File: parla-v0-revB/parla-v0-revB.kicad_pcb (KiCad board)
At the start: 2 copper layers, 70 x 70 mm, 0 parts

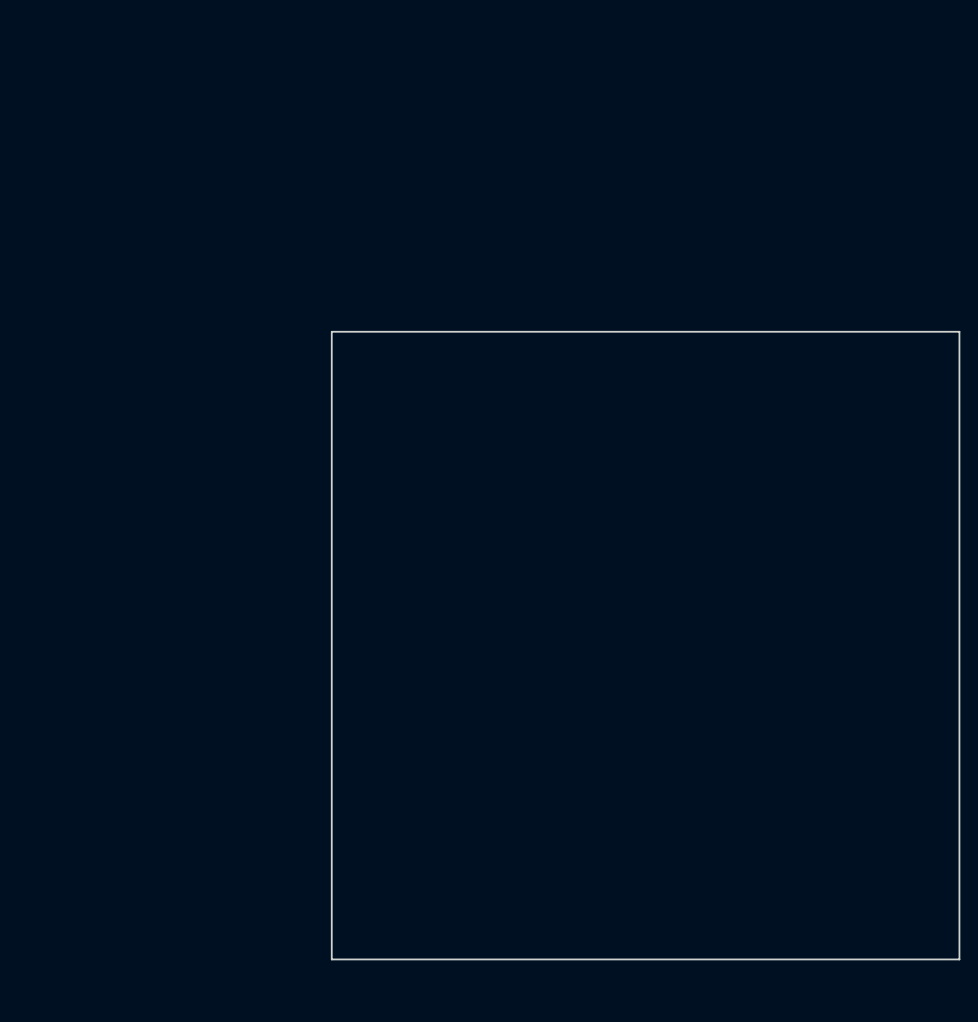
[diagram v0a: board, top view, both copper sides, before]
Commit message: agregar vias
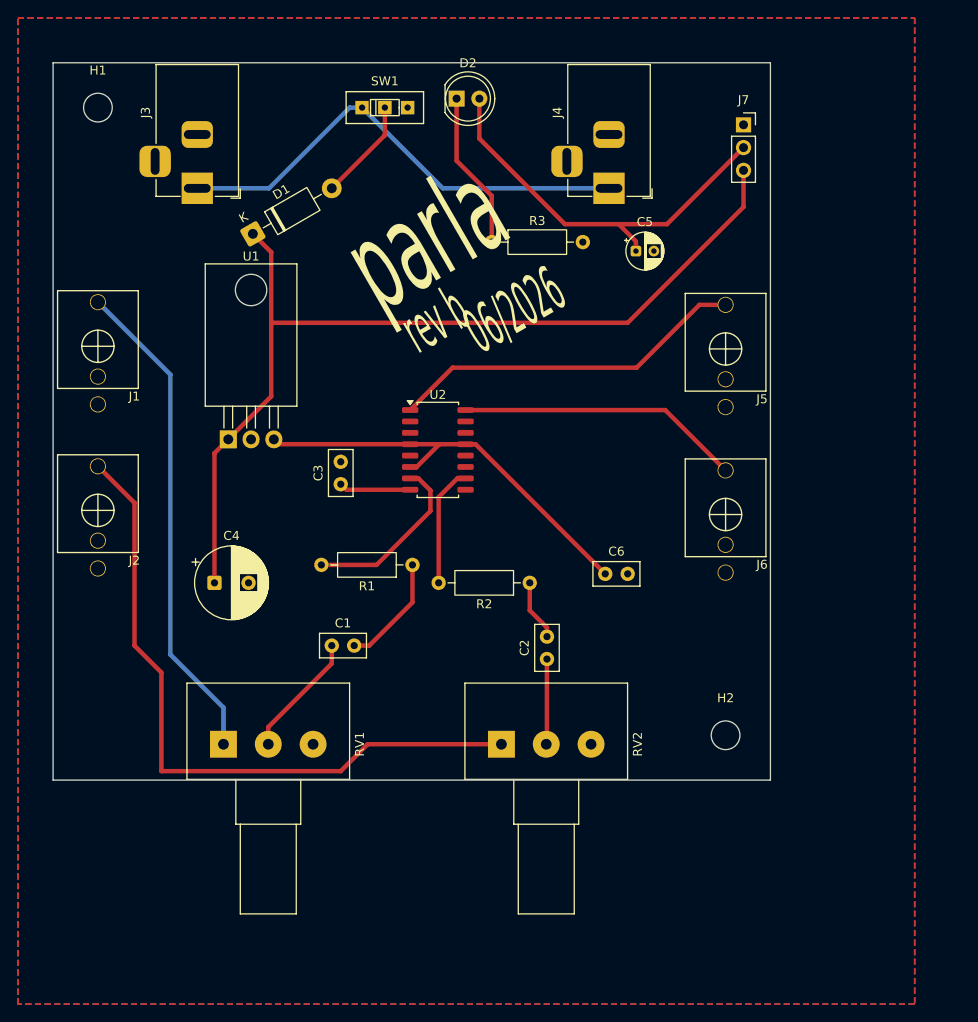
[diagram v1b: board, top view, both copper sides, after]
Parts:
- added C1: 470n, Capacitor_THT:C_Disc_D5.0mm_W2.5mm_P2.50mm, F.Cu at (50.0, 85.0)
- added C2: 470n, Capacitor_THT:C_Disc_D5.0mm_W2.5mm_P2.50mm, F.Cu at (74.0, 86.5)
- added C3: 100n, Capacitor_THT:C_Disc_D5.0mm_W2.5mm_P2.50mm, F.Cu at (51.0, 67.0)
- added C4: 100u, Capacitor_THT:CP_Radial_D8.0mm_P3.80mm, F.Cu at (36.9, 78.0)
- added C5: 10u, Capacitor_THT:CP_Radial_D4.0mm_P2.00mm, F.Cu at (83.9, 41.0)
- added C6: 100n, Capacitor_THT:C_Disc_D5.0mm_W2.5mm_P2.50mm, F.Cu at (80.5, 77.0)
- added D1: 1N4007, Diode_THT:D_DO-41_SOD81_P10.16mm_Horizontal, F.Cu at (41.2, 39.1)
- added D2: LED, LED_THT:LED_D5.0mm, F.Cu at (63.9, 24.0)
- added H1: M3, MountingHole:MountingHole_3.2mm_M3, F.Cu at (23.9, 25.0)
- added H2: M3, MountingHole:MountingHole_3.2mm_M3, F.Cu at (93.9, 95.0)
- added J1: AudioJack2_SwitchT, parla:PJ301M-12, F.Cu at (23.9, 51.6)
- added J2: AudioJack2_SwitchT, parla:PJ301M-12, F.Cu at (23.9, 69.9)
- added J3: Barrel_Jack_Switch, Connector_BarrelJack:BarrelJack_Horizontal, F.Cu at (35.0, 34.0)
- added J4: Barrel_Jack_Switch, Connector_BarrelJack:BarrelJack_Horizontal, F.Cu at (80.9, 34.0)
- added J5: AudioJack2_SwitchT, parla:PJ301M-12, F.Cu at (93.9, 51.9)
- added J6: AudioJack2_SwitchT, parla:PJ301M-12, F.Cu at (93.9, 70.4)
- added J7: Conn_01x03_Pin, Connector_PinSocket_2.54mm:PinSocket_1x03_P2.54mm_Vertical, F.Cu at (95.9, 26.9)
- added R1: 10k, Resistor_THT:R_Axial_DIN0207_L6.3mm_D2.5mm_P10.16mm_Horizontal, F.Cu at (59.0, 76.0)
- added R2: 10k, Resistor_THT:R_Axial_DIN0207_L6.3mm_D2.5mm_P10.16mm_Horizontal, F.Cu at (72.1, 78.0)
- added R3: 1k, Resistor_THT:R_Axial_DIN0207_L6.3mm_D2.5mm_P10.16mm_Horizontal, F.Cu at (67.8, 40.0)
- added RV1: 50k, Potentiometer_THT:Potentiometer_Alps_RK163_Single_Horizontal, F.Cu at (37.9, 96.0)
- added RV2: 50k, Potentiometer_THT:Potentiometer_Alps_RK163_Single_Horizontal, F.Cu at (68.9, 96.0)
- added SW1: SW_SPDT, parla:spdt_ssd12d00g3, F.Cu at (55.9, 25.0)
- added U1: L7805, Package_TO_SOT_THT:TO-220-3_Horizontal_TabDown, F.Cu at (38.5, 62.0)
- added U2: PAM8403D, Package_SO:SOP-16_4.4x10.4mm_P1.27mm, F.Cu at (61.8, 63.2)
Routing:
- net +12V: track 0.00 -> 104.5 mm
- net +5V: track 0.00 -> 92.7 mm
- net Net-(J2-Pad3): track 0.00 -> 76.1 mm
- net Net-(J1-Pad3): track 0.00 -> 55.1 mm
- net Net-(SW1-A): track 0.00 -> 53.4 mm
- net Net-(U2-LOUT+): track 0.00 -> 40.0 mm
- net Net-(U2-ROUT+): track 0.00 -> 31.8 mm
- net Net-(U2-INL): track 0.00 -> 19.8 mm
- net Net-(D2-K): track 0.00 -> 17.6 mm
- net Net-(C1-Pad1): track 0.00 -> 13.9 mm
- net Net-(U2-INR): track 0.00 -> 13.4 mm
- net Net-(C1-Pad2): track 0.00 -> 12.7 mm
- net Net-(D1-A): track 0.00 -> 11.5 mm
- net Net-(C2-Pad1): track 0.00 -> 9.53 mm
- net Net-(U2-VREF): track 0.00 -> 8.00 mm
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- added copper zone on B.Cu, net GND
- added copper zone on F.Cu, net GND
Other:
- board size 70 x 70 mm -> 80 x 80 mm
- board text added: "06/2026"
- board text added: "parla"
- board text added: "rev b"

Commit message: nueva version matias
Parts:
- removed D2: LED, LED_THT:LED_D5.0mm
- removed J6: AudioJack2_SwitchT, parla:PJ301M-12
- removed J7: Conn_01x03_Pin, Connector_PinSocket_2.54mm:PinSocket_1x03_P2.54mm_Vertical
- removed R1, R2: 10k, Resistor_THT:R_Axial_DIN0207_L6.3mm_D2.5mm_P10.16mm_Horizontal
- removed SW1: SW_SPDT, parla:spdt_ssd12d00g3
- added C10: 100n, Capacitor_SMD:C_0805_2012Metric_Pad1.18x1.45mm_HandSolder, F.Cu at (77.9, 59.6)
- added C7: 100u, Capacitor_SMD:CP_Elec_6.3x7.7, F.Cu at (71.8, 67.2)
- added C8: 220u, Capacitor_SMD:CP_Elec_6.3x5.4, F.Cu at (79.0, 67.2)
- added C9: 10u, Capacitor_SMD:CP_Elec_4x5.4, F.Cu at (82.4, 81.0)
- added D8: LED, LED_THT:LED_D5.0mm, F.Cu at (55.2, 63.2)
- added H3: M3, MountingHole:MountingHole_3.2mm_M3, F.Cu at (55.0, 95.0)
- added H4: M3, MountingHole:MountingHole_3.2mm_M3, F.Cu at (95.0, 95.0)
- added R4: 10k, Resistor_SMD:R_0805_2012Metric_Pad1.20x1.40mm_HandSolder, F.Cu at (90.7, 86.6)
- added R5: 1k, Resistor_SMD:R_0805_2012Metric_Pad1.20x1.40mm_HandSolder, F.Cu at (64.8, 65.7)
- added SW3: SW_SPDT, dis8644:spdt_ssd12d00g3, F.Cu at (78.5, 53.0)
- C1, C2: footprint Capacitor_THT:C_Disc_D5.0mm_W2.5mm_P2.50mm -> Capacitor_SMD:C_Elec_4x5.4
- C3: footprint Capacitor_THT:C_Disc_D5.0mm_W2.5mm_P2.50mm -> Capacitor_SMD:C_0805_2012Metric_Pad1.18x1.45mm_HandSolder
- C4: value 100u -> 1u; footprint Capacitor_THT:CP_Radial_D8.0mm_P3.80mm -> Capacitor_SMD:C_0805_2012Metric_Pad1.18x1.45mm_HandSolder
- C5: value 10u -> 1u; footprint Capacitor_THT:CP_Radial_D4.0mm_P2.00mm -> Capacitor_SMD:C_0805_2012Metric_Pad1.18x1.45mm_HandSolder
- C6: value 100n -> 1u; footprint Capacitor_THT:C_Disc_D5.0mm_W2.5mm_P2.50mm -> Capacitor_SMD:C_0805_2012Metric_Pad1.18x1.45mm_HandSolder
- D1: footprint Diode_THT:D_DO-41_SOD81_P10.16mm_Horizontal -> Diode_SMD:D_SOD-323_HandSoldering
- J1, J2: footprint parla:PJ301M-12 -> dis8644:PJ301M-12-T_TN_S
- J3, J4: value Barrel_Jack_Switch -> AudioJack2_SwitchT; footprint Connector_BarrelJack:BarrelJack_Horizontal -> dis8644:PJ301M-12-T_TN_S
- J5: value AudioJack2_SwitchT -> Barrel_Jack_Switch; footprint parla:PJ301M-12 -> Connector_BarrelJack:BarrelJack_Horizontal
- R3: value 1k -> 10k; footprint Resistor_THT:R_Axial_DIN0207_L6.3mm_D2.5mm_P10.16mm_Horizontal -> Resistor_SMD:R_0805_2012Metric_Pad1.20x1.40mm_HandSolder
- RV1, RV2: footprint Potentiometer_THT:Potentiometer_Alps_RK163_Single_Horizontal -> Potentiometer_THT:Potentiometer_Bourns_PTV09A-1_Single_Vertical
- U1: value L7805 -> PAM8403D; footprint Package_TO_SOT_THT:TO-220-3_Horizontal_TabDown -> Package_SO:SOP-16_4.4x10.4mm_P1.27mm
- U2: value PAM8403D -> L7805; footprint Package_SO:SOP-16_4.4x10.4mm_P1.27mm -> Package_TO_SOT_SMD:TO-252-2
- moved J1 71.3 mm to (92.8, 70.2), turned to -90 degrees
- moved J2 69.5 mm to (92.8, 79.6), turned to -90 degrees
- moved J4 51.4 mm to (56.8, 79.5), turned to 90 degrees
- moved R3 43.4 mm to (64.1, 83.2)
- moved H1 43.2 mm to (55.0, 55.0)
- moved J3 42.2 mm to (56.8, 70.0), turned to 90 degrees
- moved H2 40.0 mm to (95.0, 55.0)
- moved U1 39.7 mm to (74.9, 77.8)
- moved D1 37.8 mm to (74.0, 57.9), turned to 90 degrees
- moved C5 33.9 mm to (81.3, 74.8), turned to -90 degrees
- moved RV1 32.2 mm to (70.1, 98.0)
- moved C4 31.5 mm to (68.3, 75.8), turned to -90 degrees
- moved J5 29.4 mm to (66.0, 61.0), turned to -90 degrees
- moved U2 26.3 mm to (87.1, 55.9), turned to 90 degrees
- moved C3 22.4 mm to (68.3, 81.2)
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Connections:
- C3 pad 1: Net-(U2-VREF) -> Net-(U1-VREF)
- C4 pad 1: +12V -> GND
- C4 pad 2: GND -> +5V
- C5 pad 1: +5V -> GND
- C5 pad 2: GND -> +5V
- C6 pad 1: +5V -> GND
- C6 pad 2: GND -> +5V
- J5 pad 1: GND -> Net-(SW3-A)
- J5 pad 2: unconnected-(J5-Pad2) -> GND
- J5 pad 3: Net-(U2-LOUT+) -> unconnected-(J5-Pad3)
- R3 pad 1: Net-(D2-K) -> Net-(C1-Pad2)
- R3 pad 2: GND -> Net-(U1-INL)
- RV1 pad 1: Net-(J1-Pad3) -> Net-(J3-PadT)
- RV2 pad 1: Net-(J2-Pad3) -> Net-(J4-PadT)
- U1 pad 1: +12V -> Net-(U1-LOUT+)
- U1 pad 3: +5V -> GND
- U2 pad 1: Net-(U2-LOUT+) -> +12V
- U2 pad 3: GND -> +5V
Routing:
- net +12V: track 104.5 -> 20.4 mm
- net Net-(J2-Pad3): track 76.1 -> 0.00 mm
- net Net-(J1-Pad3): track 55.1 -> 0.00 mm
- net Net-(SW1-A): track 53.4 -> 0.00 mm
- net Net-(J4-PadT): track 0.00 -> 44.1 mm
- net Net-(U2-LOUT+): track 40.0 -> 0.00 mm
- net Net-(J3-PadT): track 0.00 -> 39.3 mm
- net Net-(U1-LOUT+): track 0.00 -> 38.6 mm, vias 0 -> 1
- net Net-(U2-ROUT+): track 31.8 -> 0.00 mm
- net Net-(U1-ROUT+): track 0.00 -> 30.1 mm, vias 0 -> 1
- net Net-(U1-INR): track 0.00 -> 21.6 mm, vias 0 -> 2
- net Net-(U2-INL): track 19.8 -> 0.00 mm
- net GND: track 0.00 -> 18.2 mm
- net Net-(D2-K): track 17.6 -> 0.00 mm
- net Net-(U1-INL): track 0.00 -> 14.5 mm
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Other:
- board size 80 x 80 mm -> 50 x 50 mm
- board text added: "IN"
- board text added: "L"
- board text added: "OUT"
- board text added: "PARLA"
- board text added: "R"
- board text added: "rev B 06-2026"
- board text removed: "06/2026"
- board text removed: "parla"
- board text removed: "rev b"

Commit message: editadas huellas standard
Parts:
- C7: footprint Capacitor_SMD:CP_Elec_6.3x7.7 -> Capacitor_SMD:CP_Elec_5x5.4
- C8: footprint Capacitor_SMD:CP_Elec_6.3x5.4 -> Capacitor_SMD:CP_Elec_6.3x7.7
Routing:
- net Net-(U1-LOUT+): track 38.6 -> 41.8 mm
- net +12V: track 20.4 -> 20.9 mm
